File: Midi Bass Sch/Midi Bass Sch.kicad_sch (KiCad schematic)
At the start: 9 parts

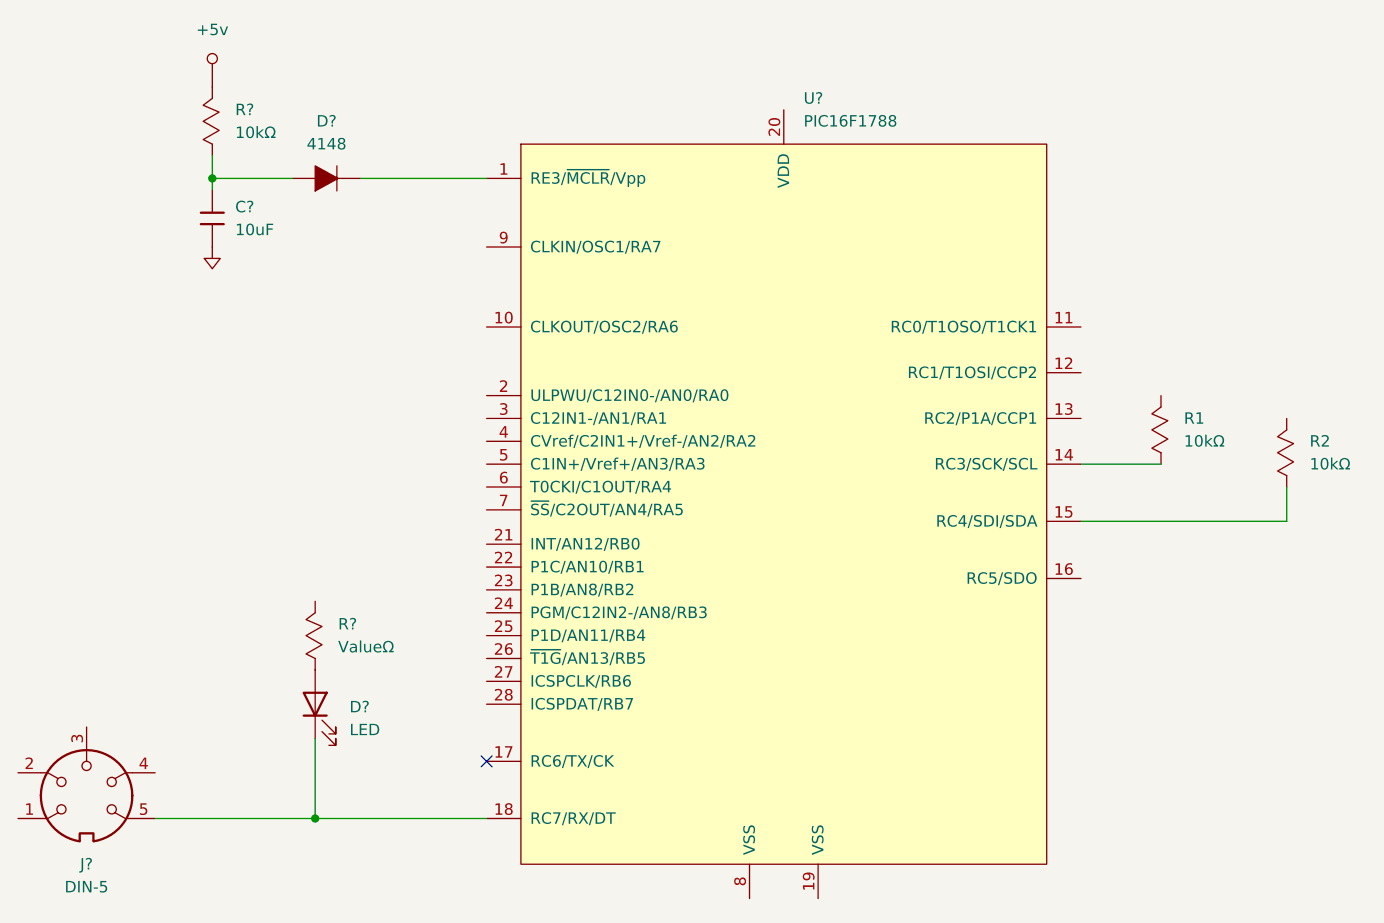
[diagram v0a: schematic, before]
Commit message: modified schematic to include seperate sheets for master and slaves
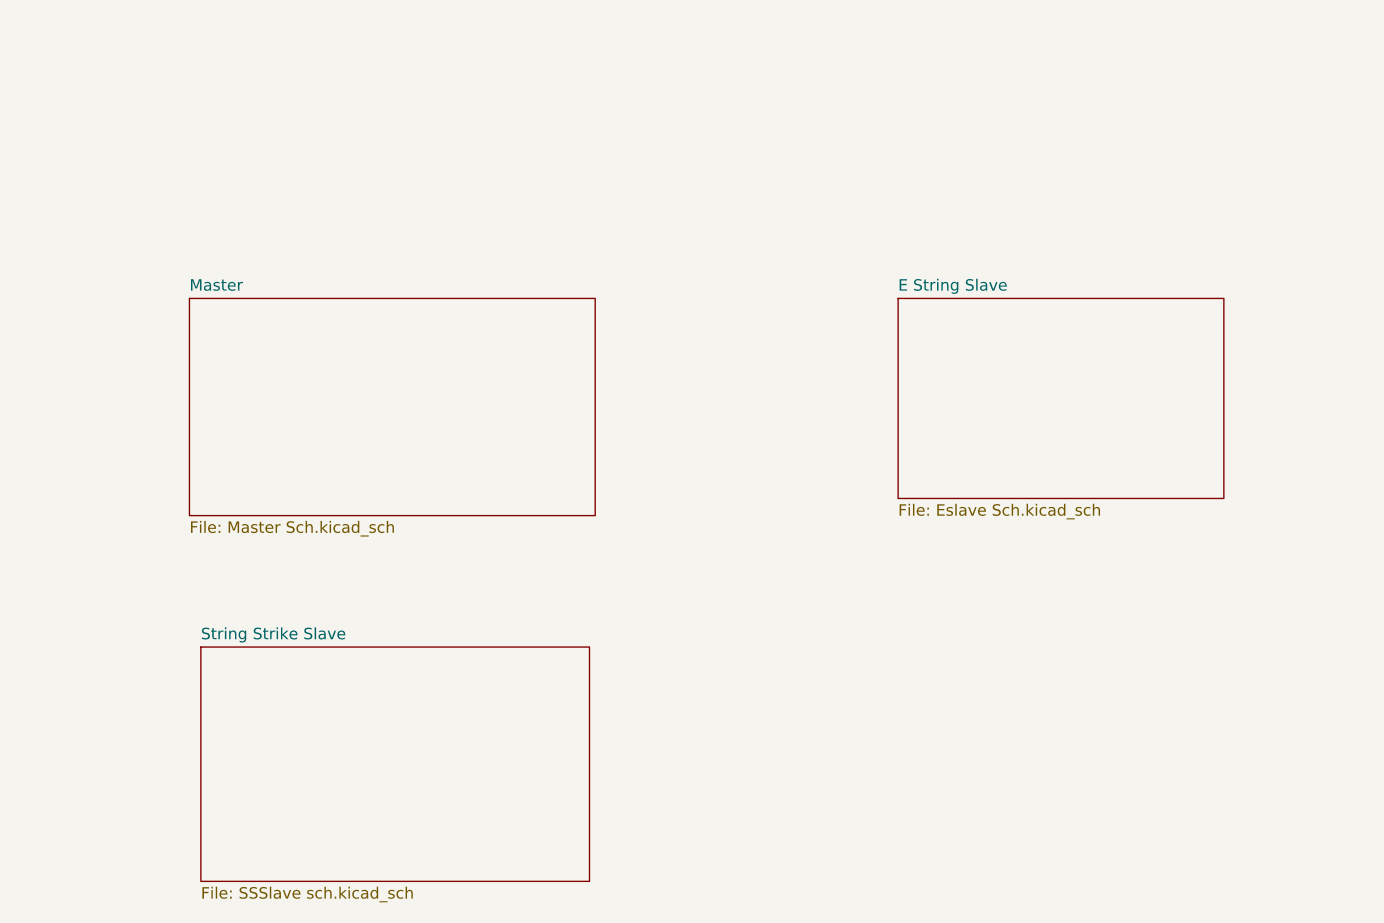
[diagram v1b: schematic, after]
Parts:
- removed C?: 10uF, symbol Owen's Symbols:Capacitor
- removed D?: LED, symbol Device:LED
- removed D?: 4148, symbol Owen's Symbols:Diode
- removed J?: DIN-5, symbol Connector:DIN-5
- removed R1, R2, R?: 10kΩ, symbol Owen's Symbols:Resistor_Mod
- removed R?: ValueΩ, symbol Owen's Symbols:Resistor_Mod
- removed U?: PIC16F1788, symbol Owen's Symbols:PIC16F1788
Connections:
- no-connect marks 1 -> 0
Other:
- added sheet E String Slave (Eslave Sch.kicad_sch)
- added sheet Master (Master Sch.kicad_sch)
- added sheet String Strike Slave (SSSlave sch.kicad_sch)
